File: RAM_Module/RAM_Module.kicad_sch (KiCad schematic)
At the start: 1 part

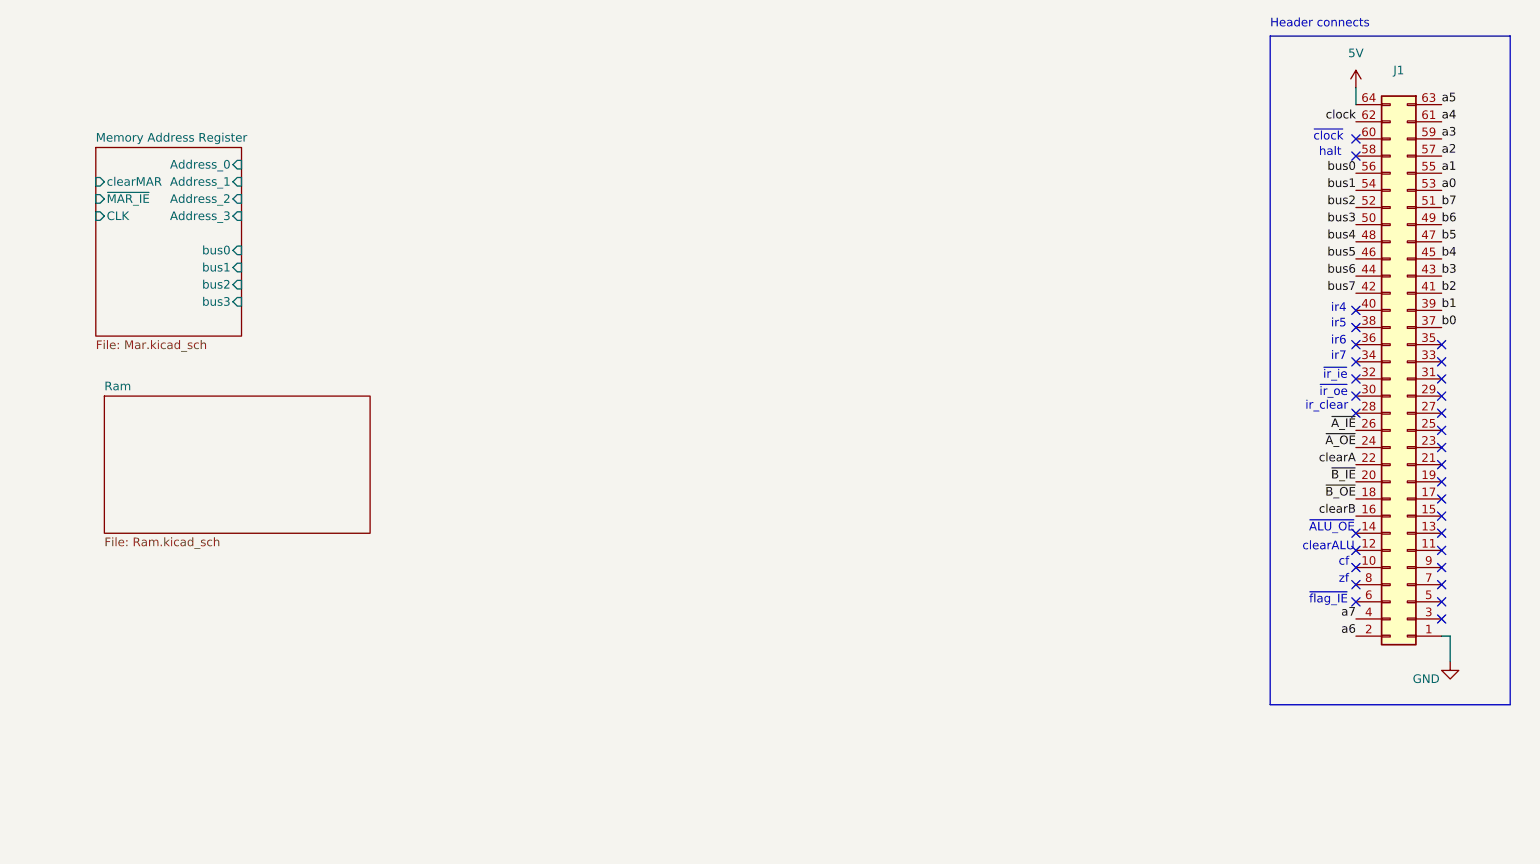
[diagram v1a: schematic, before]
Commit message: updated RAM, changed bus alignment in ALU, RAM, and registers
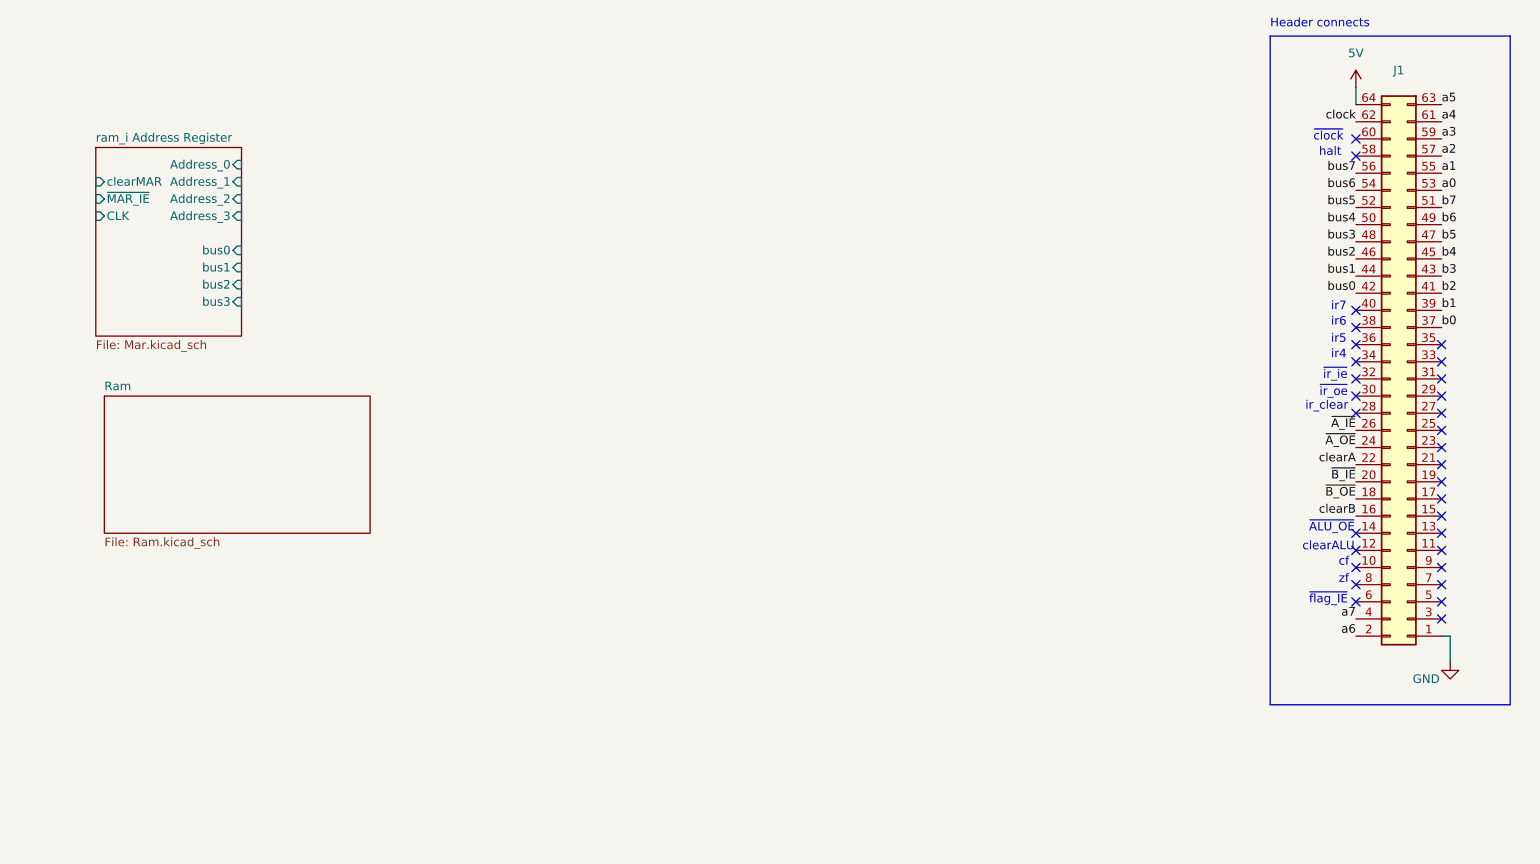
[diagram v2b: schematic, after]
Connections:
- net bus0: now also J1.42; no longer J1.56
- net bus1: now also J1.44; no longer J1.54
- net bus2: now also J1.46; no longer J1.52
- net bus3: now also J1.48; no longer J1.50
- net bus4: now also J1.50; no longer J1.48
- net bus5: now also J1.52; no longer J1.46
- net bus6: now also J1.54; no longer J1.44
- net bus7: now also J1.56; no longer J1.42
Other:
- sheet Memory Address Register renamed ram_i Address Register
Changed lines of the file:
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@@
 	(text "ir7"
 		(exclude_from_sim no)
-		(at 215.9 81.788 0)
+		(at 215.9 74.422 0)
 		(effects
 			(font
@@
 	(text "ir5"
 		(exclude_from_sim no)
-		(at 215.9 76.962 0)
+		(at 215.9 79.248 0)
 		(effects
 			(font
@@
 	(text "ir6"
 		(exclude_from_sim no)
-		(at 215.9 79.502 0)
+		(at 215.9 76.708 0)
 		(effects
 			(font
@@
 	(text "ir4"
 		(exclude_from_sim no)
-		(at 215.9 74.676 0)
+		(at 215.9 81.534 0)
 		(effects
 			(font
@@
 		)
 	)
-	(label "bus6"
-		(at 218.44 69.85 180)
-		(effects
-			(font
-				(size 1.27 1.27)
-			)
-			(justify right bottom)
-		)
-	)
-	(label "bus0"
-		(at 218.44 54.61 180)
-		(effects
-			(font
-				(size 1.27 1.27)
-			)
-			(justify right bottom)
-		)
-	)
-	(label "bus5"
-		(at 218.44 67.31 180)
+	(label "bus3"
+		(at 218.44 64.77 180)
 		(effects
 			(font
@@
 		)
 	)
+	(label "bus7"
+		(at 218.44 54.61 180)
+		(effects
+			(font
+				(size 1.27 1.27)
+			)
+			(justify right bottom)
+		)
+	)
 	(label "b3"
 		(at 231.14 69.85 0)
@@
 		)
 	)
+	(label "bus5"
+		(at 218.44 59.69 180)
+		(effects
+			(font
+				(size 1.27 1.27)
+			)
+			(justify right bottom)
+		)
+	)
+	(label "bus2"
+		(at 218.44 67.31 180)
+		(effects
+			(font
+				(size 1.27 1.27)
+			)
+			(justify right bottom)
+		)
+	)
 	(label "~{A_OE}"
 		(at 218.44 95.25 180)
@@
 		)
 	)
+	(label "bus4"
+		(at 218.44 62.23 180)
+		(effects
+			(font
+				(size 1.27 1.27)
+			)
+			(justify right bottom)
+		)
+	)
 	(label "b4"
 		(at 231.14 67.31 0)
@@
 		)
 	)
-	(label "bus3"
-		(at 218.44 62.23 180)
-		(effects
-			(font
-				(size 1.27 1.27)
-			)
-			(justify right bottom)
-		)
-	)
-	(label "bus7"
-		(at 218.44 72.39 180)
-		(effects
-			(font
-				(size 1.27 1.27)
-			)
-			(justify right bottom)
-		)
-	)
-	(label "bus4"
-		(at 218.44 64.77 180)
+	(label "bus6"
+		(at 218.44 57.15 180)
+		(effects
+			(font
+				(size 1.27 1.27)
+			)
+			(justify right bottom)
+		)
+	)
+	(label "bus1"
+		(at 218.44 69.85 180)
 		(effects
 			(font
@@
 		)
 	)
+	(label "bus0"
+		(at 218.44 72.39 180)
+		(effects
+			(font
+				(size 1.27 1.27)
+			)
+			(justify right bottom)
+		)
+	)
 	(label "b5"
 		(at 231.14 64.77 0)
@@
 			)
 			(justify left bottom)
-		)
-	)
-	(label "bus2"
-		(at 218.44 59.69 180)
-		(effects
-			(font
-				(size 1.27 1.27)
-			)
-			(justify right bottom)
-		)
-	)
-	(label "bus1"
-		(at 218.44 57.15 180)
-		(effects
-			(font
-				(size 1.27 1.27)
-			)
-			(justify right bottom)
 		)
 	)
@@
 			(color 0 0 0 0.0000)
 		)
-		(property "Sheetname" "Memory Address Register"
+		(property "Sheetname" "ram_i Address Register"
 			(at 31.75 50.0884 0)
 			(effects

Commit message: fixed Ram register, fixed mar in ram.v, updated caps in alu, ram, and instruction register
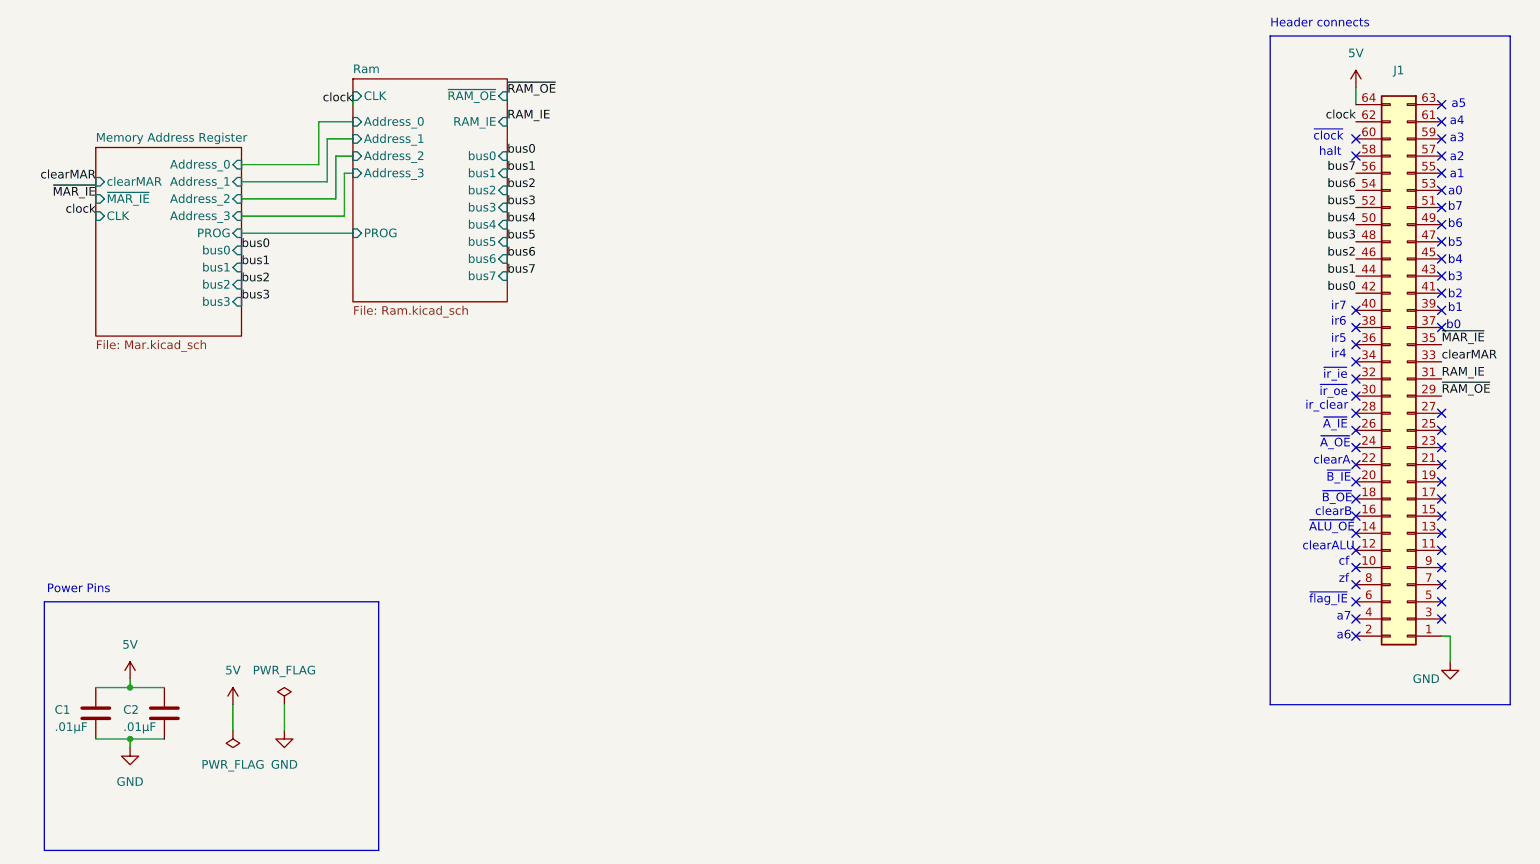
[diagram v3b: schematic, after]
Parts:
- added C1, C2: .01µF, Capacitor_THT:C_Disc_D5.0mm_W2.5mm_P2.50mm, symbol Device:C
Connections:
- net 5V: now also C1.2, C2.2
- net GND: now also C1.1, C2.1
- net ~{RAM_OE}: now reaches J1.29
- net RAM_IE: now reaches J1.31
- net clearMAR: now reaches J1.33
- net ~{MAR_IE}: now reaches J1.35
- net a0: no longer names the net of J1.53
- net a1: no longer names the net of J1.55
- net a2: no longer names the net of J1.57
- net a3: no longer names the net of J1.59
- net a4: no longer names the net of J1.61
- net a5: no longer names the net of J1.63
- net a6: no longer names the net of J1.2
- net a7: no longer names the net of J1.4
- net b0: no longer names the net of J1.37
- net b1: no longer names the net of J1.39
- net b2: no longer names the net of J1.41
- net b3: no longer names the net of J1.43
- net b4: no longer names the net of J1.45
- net b5: no longer names the net of J1.47
- net b6: no longer names the net of J1.49
- net b7: no longer names the net of J1.51
- net clearA: no longer names the net of J1.22
- net clearB: no longer names the net of J1.16
- net ~{A_IE}: no longer names the net of J1.26
- net ~{A_OE}: no longer names the net of J1.24
- net ~{B_IE}: no longer names the net of J1.20
- net ~{B_OE}: no longer names the net of J1.18
- no-connect marks 31 -> 49
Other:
- sheet ram_i Address Register renamed Memory Address Register
- sheet Memory Address Register ports: added PROG; removed none
- sheet Ram ports: added Address_0, Address_1, Address_2, Address_3, CLK, PROG, RAM_IE, bus0, bus1, bus2, bus3, bus4, bus5, bus6, bus7, ~{RAM_OE}; removed none
- note added: "Power Pins"
- note added: "a0"
- note added: "a1"
- note added: "a2"
- note added: "a3"
- note added: "a4"
- note added: "a5"
- note added: "a6"
- note added: "a7"
- note added: "b0"
- note added: "b1"
- note added: "b2"
- note added: "b3"
- note added: "b4"
- note added: "b5"
- note added: "b6"
- note added: "b7"
- note added: "clearA"
- note added: "clearB"
- note added: "~{A_IE}"
- note added: "~{A_OE}"
- note added: "~{B_IE}"
- note added: "~{B_OE}"
